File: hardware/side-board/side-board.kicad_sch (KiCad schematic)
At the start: 6 parts, among them IC14 NUP2105LT1G, IC15 NUP2105LT1G, IC6 TPS62933DRLR

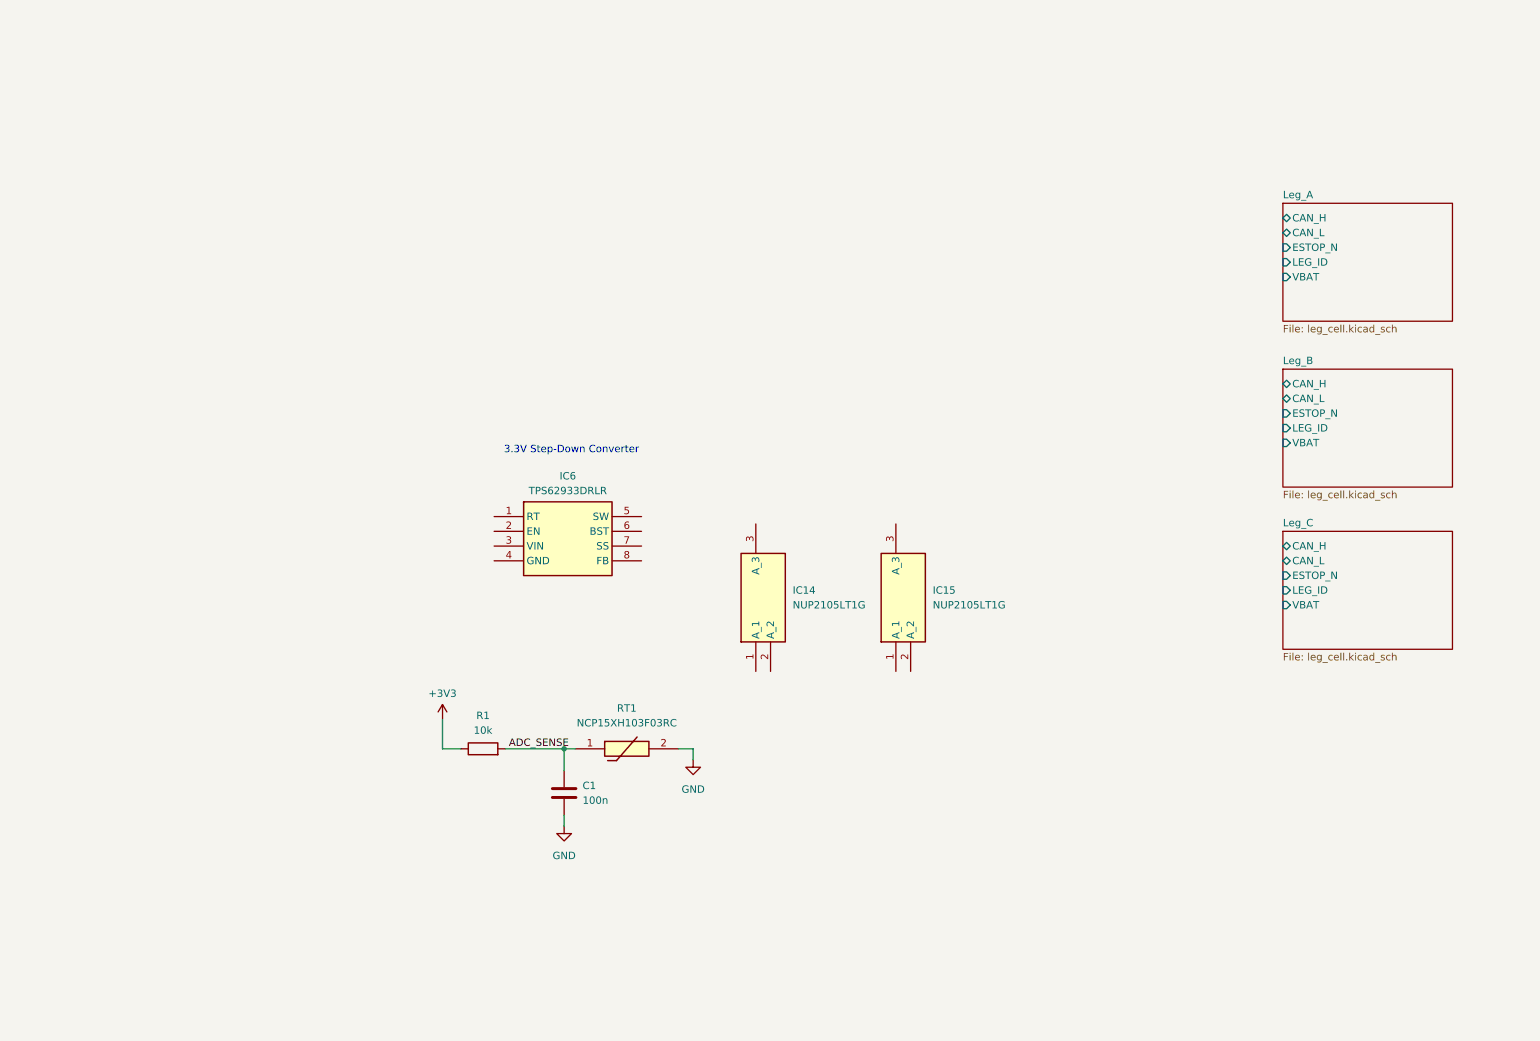
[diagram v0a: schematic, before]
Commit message: Added leg configuration bits
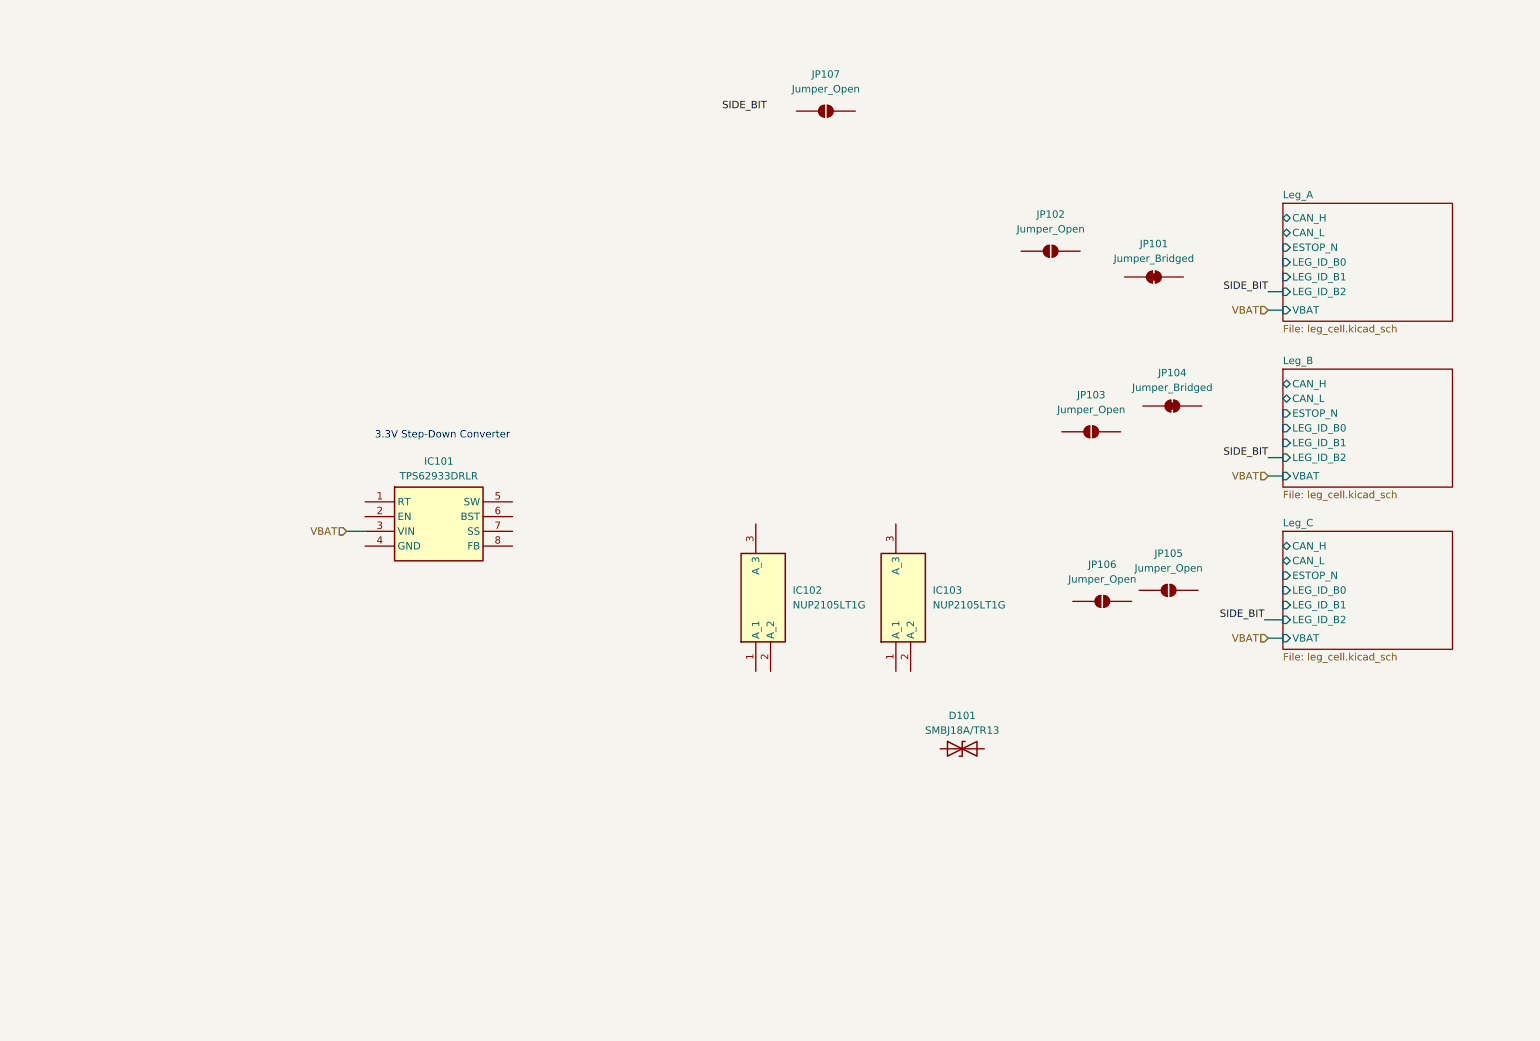
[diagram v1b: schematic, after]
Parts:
- removed C1: 100n, Capacitor_SMD:C_0603_1608Metric, symbol Device:C
- removed R1: 10k, Resistor_SMD:R_0603_1608Metric, symbol Device:R
- removed RT1: NCP15XH103F03RC, side-board:THRMC1005X55N, symbol side-board:NCP15XH103F03RC
- added D101: SMBJ18A/TR13, Diode_SMD:D_SMB, symbol Device:D_TVS
- added JP101, JP104: Jumper_Bridged, Jumper:SolderJumper-2_P1.3mm_Bridged2Bar_Pad1.0x1.5mm, symbol Jumper:SolderJumper_2_Bridged
- added JP102, JP103, JP105, JP106, JP107: Jumper_Open, Jumper:SolderJumper-2_P1.3mm_Open_Pad1.0x1.5mm, symbol Jumper:SolderJumper_2_Open
- renumbered IC6 to IC101, IC14 to IC102, IC15 to IC103
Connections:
- net VBAT: now reaches IC101.3 (VIN)
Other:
- sheet Leg_A ports: added LEG_ID_B0, LEG_ID_B1, LEG_ID_B2; removed LEG_ID
- sheet Leg_B ports: added LEG_ID_B0, LEG_ID_B1, LEG_ID_B2; removed LEG_ID
- sheet Leg_C ports: added LEG_ID_B0, LEG_ID_B1, LEG_ID_B2; removed LEG_ID
- moved on the sheet: IC101

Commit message: Gazebo tests & servo tests
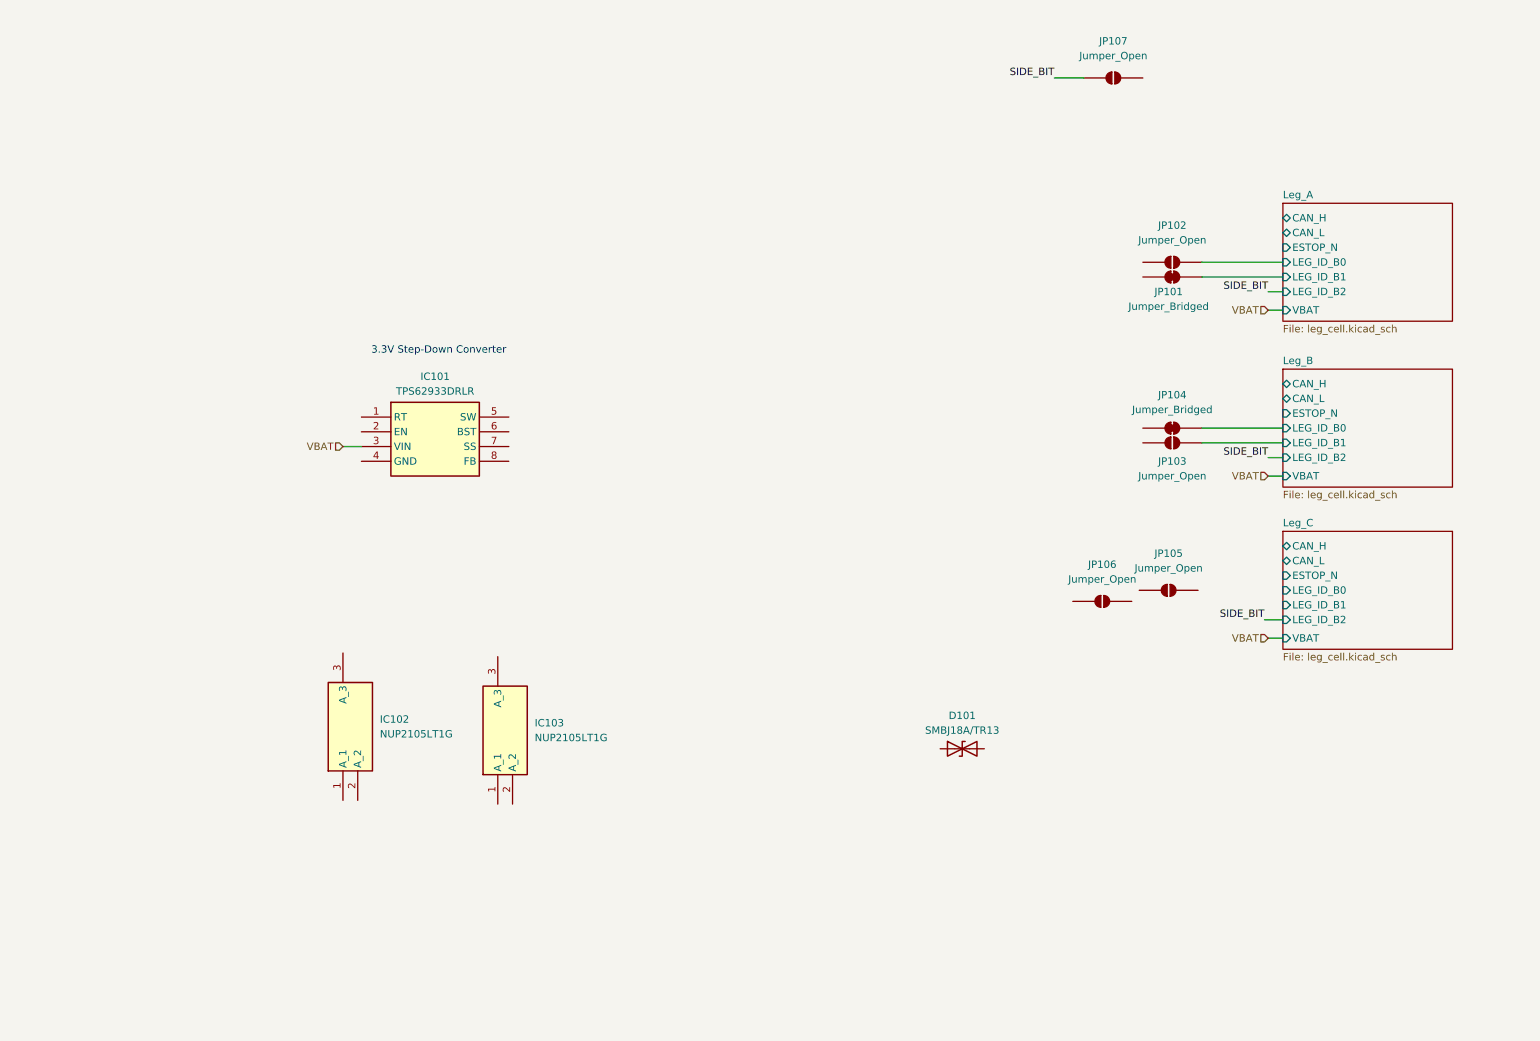
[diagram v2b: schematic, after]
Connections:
- net Leg_A/LEG_ID_B0: now also JP102.2 (B)
- net Leg_A/LEG_ID_B1: now also JP101.2 (B)
- net Leg_B/LEG_ID_B0: now also JP104.2 (B)
- net Leg_B/LEG_ID_B1: now also JP103.2 (B)
- net SIDE_BIT: now also JP107.1 (A)
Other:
- moved on the sheet: IC101, IC102, IC103, JP101, JP102, JP103, JP104, JP107

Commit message: Added TPS62933 design in schematic
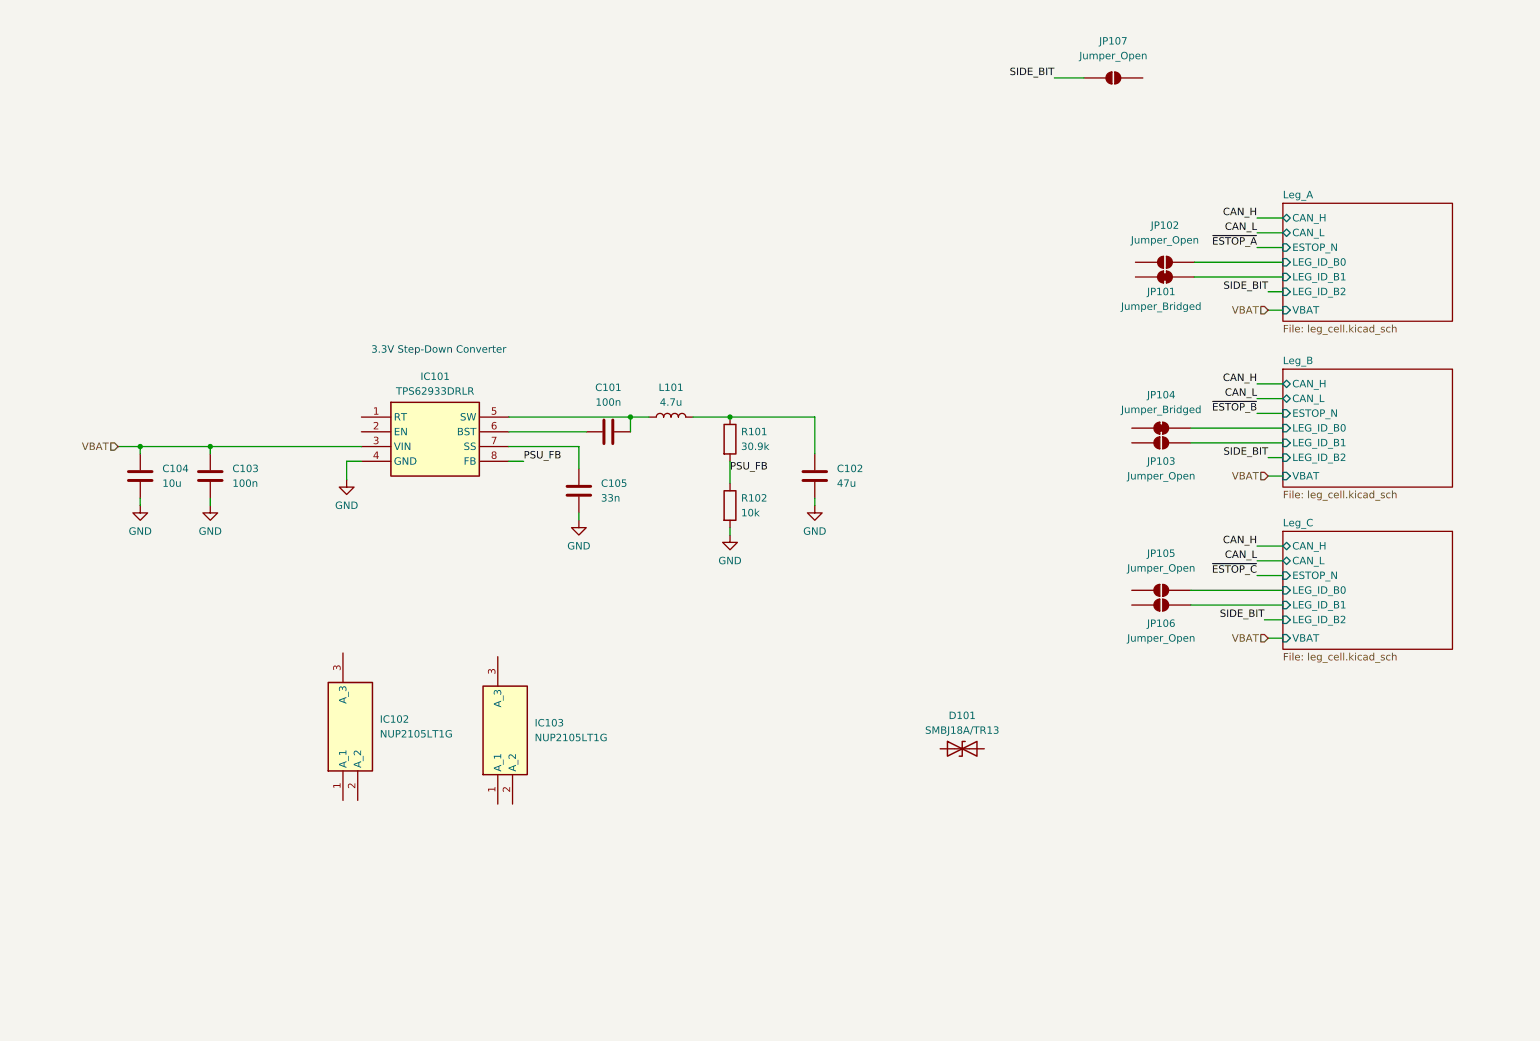
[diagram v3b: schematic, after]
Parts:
- added C101, C103: 100n, Capacitor_SMD:C_0805_2012Metric, symbol Device:C
- added C102: 47u, Capacitor_SMD:C_0805_2012Metric, symbol Device:C
- added C104: 10u, Capacitor_SMD:C_0805_2012Metric, symbol Device:C
- added C105: 33n, Capacitor_SMD:C_0805_2012Metric, symbol Device:C
- added L101: 4.7u, symbol Device:L
- added R101: 30.9k, Resistor_SMD:R_0805_2012Metric, symbol Device:R
- added R102: 10k, Resistor_SMD:R_0805_2012Metric, symbol Device:R
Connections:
- net Leg_C/LEG_ID_B0: now also JP105.2 (B)
- net Leg_C/LEG_ID_B1: now also JP106.2 (B)
- net VBAT: now also C103.2, C104.2
- net GND: now reaches IC101.4 (GND)
- net GND: now also C102.1, C103.1, C104.1, C105.1, R102.2
- net at IC101.5 (SW): now also C101.2, L101.1
- net at IC101.6 (BST): now also C101.1
- net at IC101.7 (SS): now also C105.2
- net PSU_FB: now reaches IC101.8 (FB)
- net PSU_FB: now also R101.2, R102.1
- new net: C102.2, L101.2, R101.1
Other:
- moved on the sheet: JP101, JP102, JP103, JP104, JP105, JP106

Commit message: Updated TPS62933 circuit
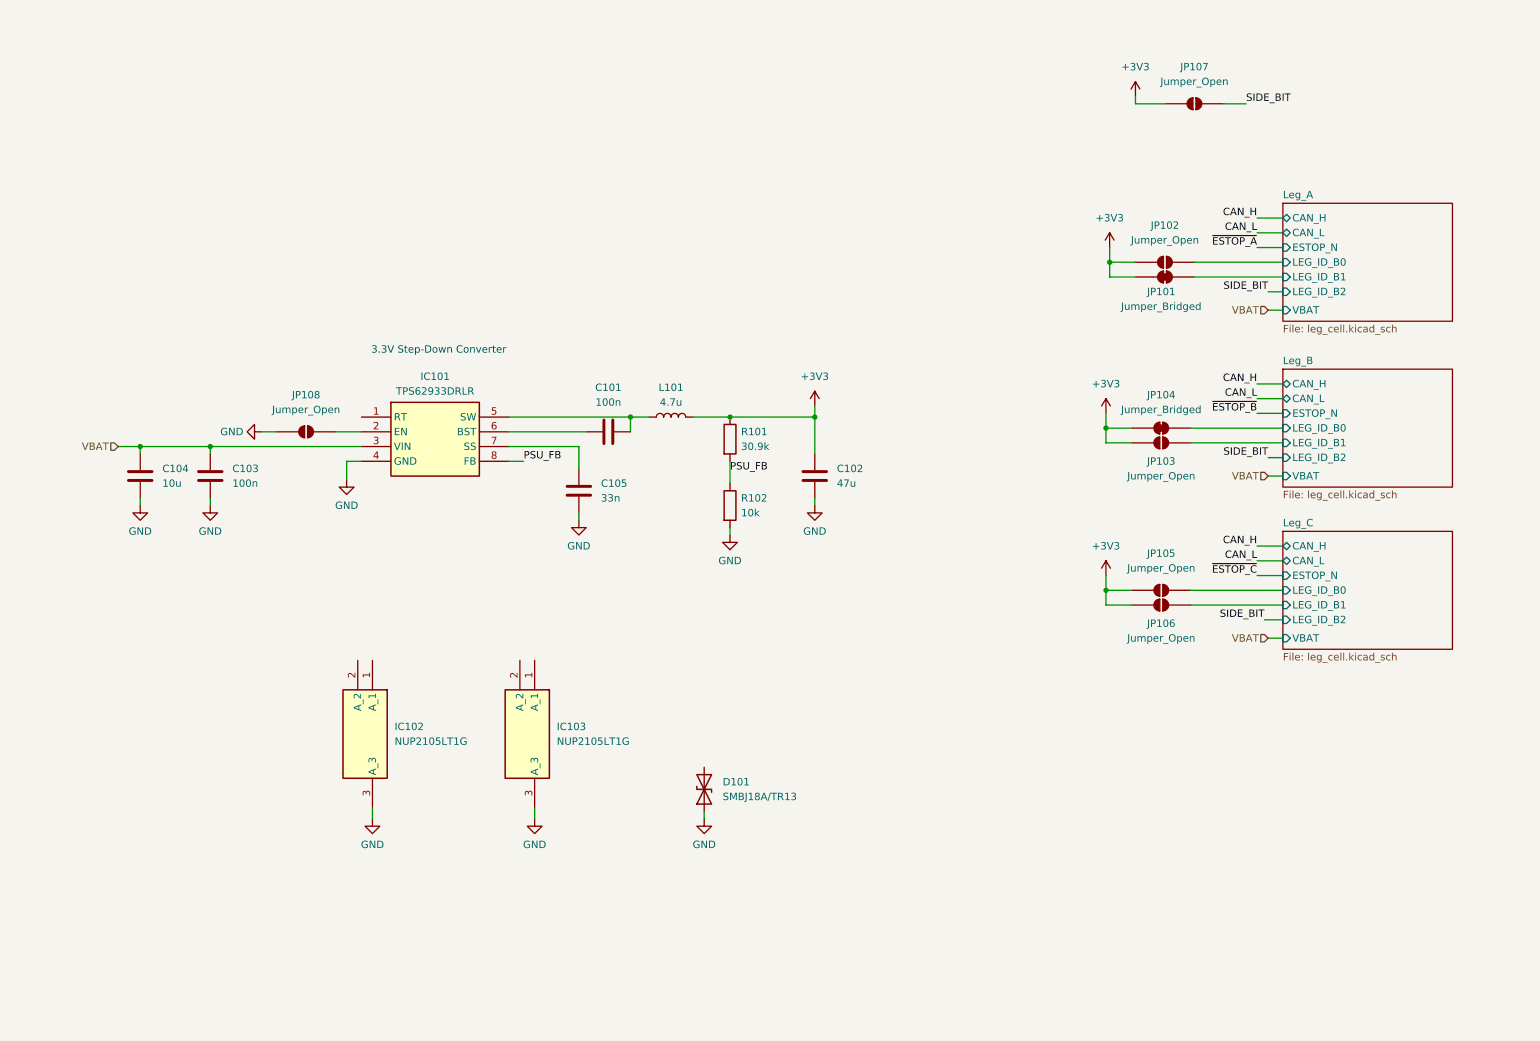
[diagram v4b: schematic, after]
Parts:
- added JP108: Jumper_Open, Jumper:SolderJumper-2_P1.3mm_Open_Pad1.0x1.5mm, symbol Jumper:SolderJumper_2_Open
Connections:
- net GND: now also D101.1 (A1), IC102.3 (A_3), IC103.3 (A_3), JP108.1 (A)
- net SIDE_BIT: now also JP107.2 (B); no longer JP107.1 (A)
- net +3V3: now reaches C102.2, L101.2, R101.1
- net +3V3: now also JP101.1 (A), JP102.1 (A), JP103.1 (A), JP104.1 (A), JP105.1 (A), JP106.1 (A), JP107.1 (A)
- net at IC101.2 (EN): now also JP108.2 (B)
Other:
- moved on the sheet: D101, IC102, IC103, JP107

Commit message: Added more leg firmware features
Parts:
- removed IC103: NUP2105LT1G, side-board:SOT96P237X111-3N, symbol side-board:NUP2105LT1G
- removed JP105, JP106: Jumper_Open, Jumper:SolderJumper-2_P1.3mm_Open_Pad1.0x1.5mm, symbol Jumper:SolderJumper_2_Open
- added D102: GREEN, LED_SMD:LED_0805_2012Metric, symbol Device:LED
- added JP105, JP106: Jumper_Bridged, Jumper:SolderJumper-2_P1.3mm_Bridged2Bar_Pad1.0x1.5mm, symbol Jumper:SolderJumper_2_Bridged
- added R103: 1k, Resistor_SMD:R_0603_1608Metric, symbol Device:R
- added TP101: CANH, TestPoint:TestPoint_Pad_D2.0mm, symbol Connector:TestPoint
- added TP102: CANL, TestPoint:TestPoint_Pad_D2.0mm, symbol Connector:TestPoint
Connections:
- net +3V3: now also JP102.2 (B), JP105.1 (A), JP106.1 (A), R103.2; no longer JP102.1 (A)
- net CAN_H: now also IC102.1 (A_1), TP101.1
- net CAN_L: now also IC102.2 (A_2), TP102.1
- net GND: now also D102.1 (K)
- net Leg_A/LEG_ID_B0: now also JP101.2 (B); no longer JP102.2 (B)
- net Leg_A/LEG_ID_B1: now also JP102.1 (A); no longer JP101.2 (B)
- net Leg_B/LEG_ID_B0: now also JP103.2 (B); no longer JP104.2 (B)
- net Leg_B/LEG_ID_B1: now also JP104.2 (B); no longer JP103.2 (B)
- net Leg_C/LEG_ID_B0: now also JP106.2 (B)
- net Leg_C/LEG_ID_B1: now also JP105.2 (B)
- net VBAT: now also D101.2 (A2)
- new net: D102.2 (A), R103.1
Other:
- sheet Leg_A ports: added ~{ESTOP}; removed ESTOP_N
- sheet Leg_B ports: added ~{ESTOP}; removed ESTOP_N
- sheet Leg_C ports: added ~{ESTOP}; removed ESTOP_N
- note added: "Watch polarity"
- moved on the sheet: C101, C102, C103, C104, C105, D101, IC101, IC102, JP108, L101, R101, R102

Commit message: Updated schematic for leg
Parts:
- removed D101: SMBJ18A/TR13, Diode_SMD:D_SMB, symbol Device:D_TVS
- added D101: SMBJ18A-E3_52, side-board:DIOM5436X244N, symbol side-board:SMBJ18A-E3_52
- added J101: Inter-board Connector, Connector_JST:JST_XH_S4B-XH-A-1_1x04_P2.50mm_Horizontal, symbol Connector_Generic:Conn_01x04
- added R104: 120, Resistor_SMD:R_0603_1608Metric, symbol Device:R
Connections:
- net CAN_H: now also J101.1 (Pin_1), R104.2
- net CAN_L: now also J101.2 (Pin_2), R104.1
- net GND: now also D101.2 (A), J101.3 (Pin_3)
- net VBAT: now also D101.1 (K)
- new net ~{ESTOP_N}: J101.4 (Pin_4)
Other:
- note removed: "Watch polarity"

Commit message: Updated side board schematic
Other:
- moved on the sheet: D101, D102, J101, R103, R104, TP101, TP102
